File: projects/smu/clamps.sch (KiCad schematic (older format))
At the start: 36 parts, among them U401 DAC8734, U402 LM324, U404 LM324, U405 DG444

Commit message: do edges again
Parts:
- added R417: 10k, Resistors_SMD:R_1206, symbol R
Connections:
- net REF_IN4 is gone; now on an unnamed net: U405.8 (IN4)
- net 3.3V: now also R417.2
- net REF_IN3: no longer names the net of U405.16 (IN3)
- net REF_IN3: now also R417.1
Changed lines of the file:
@@
 	5650 2700 5800 2700
 Wire Wire Line
-	7000 3300 7350 3300
-Wire Wire Line
 	7350 3000 7000 3000
-Wire Wire Line
-	5800 3300 5350 3300
 Wire Wire Line
 	5650 3200 5800 3200
@@
 Wire Wire Line
 	7000 2600 7350 2600
-Text GLabel 7350 3300 2    60   Input ~ 0
-REF_IN3
-Text GLabel 5350 3300 0    60   Input ~ 0
-REF_IN4
 Text GLabel 7350 3100 2    60   Input ~ 0
 AGND
@@
 Text GLabel 3000 6450 3    60   Input ~ 0
 AGND
+Text GLabel 5100 3300 0    60   Input ~ 0
+3.3V
+$Comp
+L R R417
+U 1 1 58A97CCD
+P 5400 3300
+F 0 "R417" V 5480 3300 50  0000 C CNN
+F 1 "10k" V 5400 3300 50  0000 C CNN
+F 2 "Resistors_SMD:R_1206" V 5330 3300 50  0001 C CNN
+F 3 "" H 5400 3300 50  0000 C CNN
+	1    5400 3300
+	0    1    1    0
+$EndComp
+Wire Wire Line
+	5100 3300 5250 3300
+Wire Wire Line
+	5550 3300 5800 3300
+Wire Wire Line
+	5650 3550 7150 3550
+Wire Wire Line
+	7150 3550 7150 3300
+Wire Wire Line
+	7150 3300 7000 3300
+Wire Wire Line
+	5650 3550 5650 3300
+Connection ~ 5650 3300
 $EndSCHEMATC

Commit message: update
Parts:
- renumbered D404 to D402, D402 to D403, D403 to D404, R406 to R405, R405 to R406, R412 to R410, R413 to R411, R410 to R412, R411 to R413
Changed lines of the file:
@@
 NoConn ~ 11650 3400
 $Comp
-L 1N4148 D404
+L 1N4148 D402
 U 1 1 58623121
 P 12200 3100
-F 0 "D404" V 12125 3175 40  0000 L BNN
+F 0 "D402" V 12125 3175 40  0000 L BNN
 F 1 "1N4148" H 12075 3025 40  0000 L CNN
 F 2 "Diodes_SMD:MiniMELF_Standard" H 12200 3250 30  0001 C CNN
@@
 	8300 1700 8300 3100
 $Comp
-L R R412
+L R R410
 U 1 1 58623142
 P 10300 3000
-F 0 "R412" V 10380 3000 50  0000 C CNN
+F 0 "R410" V 10380 3000 50  0000 C CNN
 F 1 "R" V 10300 3000 50  0000 C CNN
 F 2 "Resistors_SMD:R_1206" V 10230 3000 50  0001 C CNN
@@
 $EndComp
 $Comp
-L R R413
+L R R411
 U 1 1 58623149
 P 10300 3200
-F 0 "R413" V 10380 3200 50  0000 C CNN
+F 0 "R411" V 10380 3200 50  0000 C CNN
 F 1 "R" V 10300 3200 50  0000 C CNN
 F 2 "Resistors_SMD:R_1206" V 10230 3200 50  0001 C CNN
@@
 NoConn ~ 11650 4700
 $Comp
-L 1N4148 D402
+L 1N4148 D403
 U 1 1 5862319C
 P 12150 4400
-F 0 "D402" V 12075 4475 40  0000 L BNN
+F 0 "D403" V 12075 4475 40  0000 L BNN
 F 1 "1N4148" H 12025 4325 40  0000 L CNN
 F 2 "Diodes_SMD:MiniMELF_Standard" H 12150 4550 30  0001 C CNN
@@
 NoConn ~ 11650 6000
 $Comp
-L 1N4148 D403
+L 1N4148 D404
 U 1 1 586231B8
 P 12150 5700
-F 0 "D403" V 12075 5775 40  0000 L BNN
+F 0 "D404" V 12075 5775 40  0000 L BNN
 F 1 "1N4148" H 12025 5625 40  0000 L CNN
 F 2 "Diodes_SMD:MiniMELF_Standard" H 12150 5850 30  0001 C CNN
@@
 $EndComp
 $Comp
-L R R405
+L R R406
 U 1 1 586231D2
 P 8650 5700
-F 0 "R405" V 8730 5700 50  0000 C CNN
+F 0 "R406" V 8730 5700 50  0000 C CNN
 F 1 "R" V 8650 5700 50  0000 C CNN
 F 2 "Resistors_SMD:R_1206" V 8580 5700 50  0001 C CNN
@@
 Connection ~ 9650 5600
 $Comp
-L R R410
+L R R412
 U 1 1 586231E6
 P 10250 4300
-F 0 "R410" V 10330 4300 50  0000 C CNN
+F 0 "R412" V 10330 4300 50  0000 C CNN
 F 1 "R" V 10250 4300 50  0000 C CNN
 F 2 "Resistors_SMD:R_1206" V 10180 4300 50  0001 C CNN
@@
 $EndComp
 $Comp
-L R R411
+L R R413
 U 1 1 586231ED
 P 10250 4500
-F 0 "R411" V 10330 4500 50  0000 C CNN
+F 0 "R413" V 10330 4500 50  0000 C CNN
 F 1 "R" V 10250 4500 50  0000 C CNN
 F 2 "Resistors_SMD:R_1206" V 10180 4500 50  0001 C CNN
@@
 	9650 3650 9350 3650
 $Comp
-L R R406
+L R R405
 U 1 1 5862326B
 P 9200 3650
-F 0 "R406" V 9280 3650 50  0000 C CNN
+F 0 "R405" V 9280 3650 50  0000 C CNN
 F 1 "R" V 9200 3650 50  0000 C CNN
 F 2 "Resistors_SMD:R_1206" V 9130 3650 50  0001 C CNN

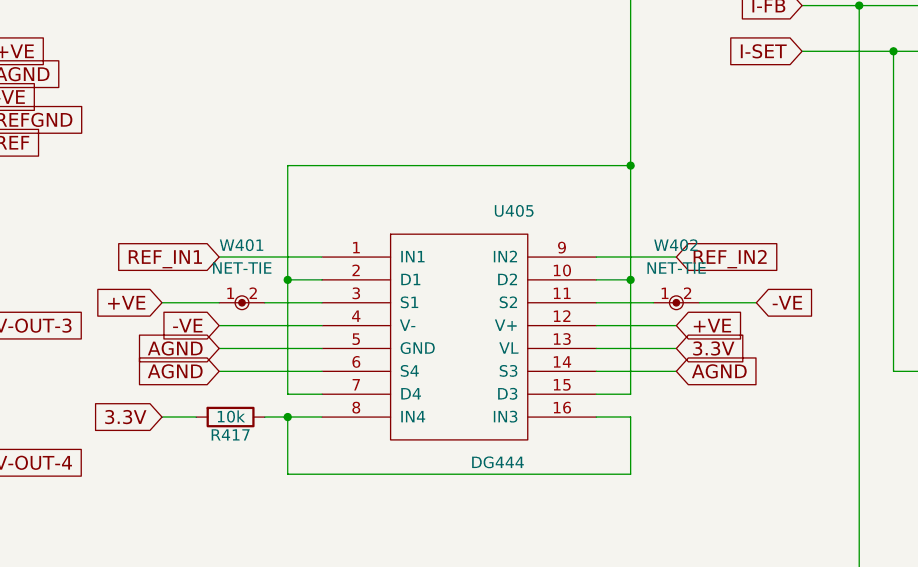
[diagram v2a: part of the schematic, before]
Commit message: add lt1021, remove net-tie
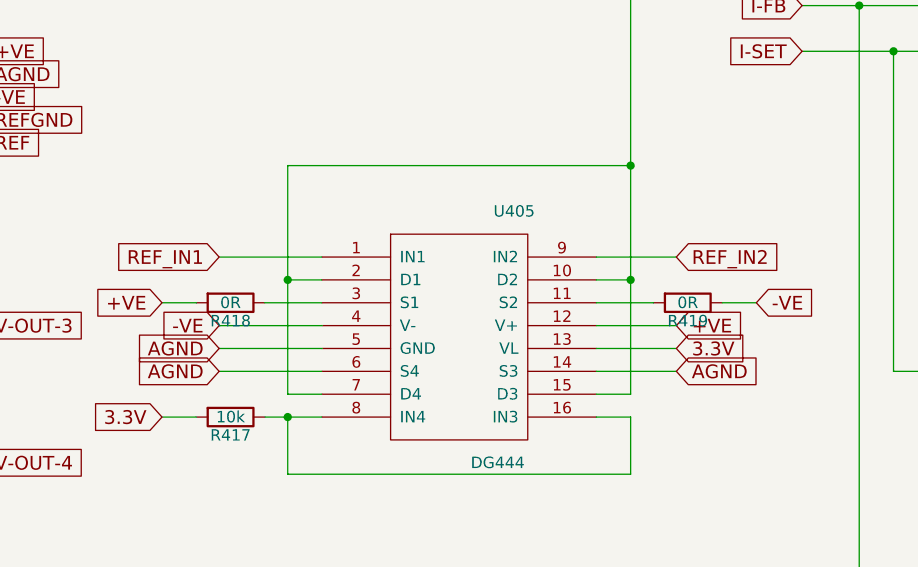
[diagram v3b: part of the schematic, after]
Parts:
- removed W401, W402: NET-TIE, footprint:NET-TIE-0.3mm, symbol NET-TIE
- added R418, R419: 0R, Resistors_SMD:R_1206, symbol R
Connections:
- net +VE: now also R418.2
- net -VE: now also R419.1
- net at U405.11 (S2): now also R419.2
- net at U405.3 (S1): now also R418.1

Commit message: update
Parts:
- added R420, R421: 5k, symbol R
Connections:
- net REF: now also R420.1; no longer U401.30 (REF-A), U401.31 (REF-B)
- net REFGND: now also R421.2
- new net: R420.2, R421.1, U401.30 (REF-A), U401.31 (REF-B)
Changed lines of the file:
@@
 Text GLabel 4300 1800 2    60   Input ~ 0
 AGND
-Text GLabel 4300 2100 2    60   Input ~ 0
+Text GLabel 5000 1600 1    60   Input ~ 0
 REF
 Text GLabel 4300 2000 2    60   Input ~ 0
@@
 	3800 2300 3650 2300
 Wire Wire Line
-	3650 2100 4300 2100
+	3650 2100 5000 2100
 Wire Wire Line
 	3700 2100 3700 2200
@@
 Wire Wire Line
 	7550 2800 7700 2800
+$Comp
+L R R420
+U 1 1 58AD4567
+P 5000 1850
+F 0 "R420" V 5080 1850 50  0000 C CNN
+F 1 "5k" V 5000 1850 50  0000 C CNN
+F 2 "" V 4930 1850 50  0000 C CNN
+F 3 "" H 5000 1850 50  0000 C CNN
+	1    5000 1850
+	1    0    0    -1
+$EndComp
+$Comp
+L R R421
+U 1 1 58AD48B2
+P 5000 2300
+F 0 "R421" V 5080 2300 50  0000 C CNN
+F 1 "5k" V 5000 2300 50  0000 C CNN
+F 2 "" V 4930 2300 50  0000 C CNN
+F 3 "" H 5000 2300 50  0000 C CNN
+	1    5000 2300
+	1    0    0    -1
+$EndComp
+Wire Wire Line
+	5000 2450 4150 2450
+Connection ~ 4150 2450
+Wire Wire Line
+	5000 2000 5000 2150
+Connection ~ 5000 2100
+Wire Wire Line
+	5000 1700 5000 1600
 $EndSCHEMATC

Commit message: add power
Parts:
- R420, R421: footprint (none) -> Resistors_SMD:R_1206
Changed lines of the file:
@@
 $Descr A3 16535 11693
 encoding utf-8
-Sheet 3 4
+Sheet 3 5
 Title ""
 Date ""
@@
 F 0 "R420" V 5080 1850 50  0000 C CNN
 F 1 "5k" V 5000 1850 50  0000 C CNN
-F 2 "" V 4930 1850 50  0000 C CNN
+F 2 "Resistors_SMD:R_1206" V 4930 1850 50  0001 C CNN
 F 3 "" H 5000 1850 50  0000 C CNN
 	1    5000 1850
@@
 F 0 "R421" V 5080 2300 50  0000 C CNN
 F 1 "5k" V 5000 2300 50  0000 C CNN
-F 2 "" V 4930 2300 50  0000 C CNN
+F 2 "Resistors_SMD:R_1206" V 4930 2300 50  0001 C CNN
 F 3 "" H 5000 2300 50  0000 C CNN
 	1    5000 2300
